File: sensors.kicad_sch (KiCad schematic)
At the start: 43 parts, among them IC1 SHT40-CD1B-R3, IC2 SGP40-D-R4, IC3 SGP40-D-R4, IC4 SGP40-D-R4, IC6 SGP40-D-R4, U2 TCA9546APWR, U3 BMP581, U4 BMP581, U5 BMP581, U6 BMP581

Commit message: feat: pullup resistors values
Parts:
- added R1: 10k, Resistor_SMD:R_0603_1608Metric, symbol Device:R
- R14, R15, R16, R17, R18, R19, R3, R4: value R -> 2k2
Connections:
- net +3V3: now also R1.1
- net ~{RESET}: now also R1.2
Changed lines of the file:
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@@
 	)
 	(junction
+		(at 328.93 143.51)
+		(diameter 0)
+		(color 0 0 0 0)
+	)
+	(junction
 		(at 193.04 242.57)
 		(diameter 0)
@@
 	(polyline
 		(pts
-			(xy 315.722 80.518) (xy 315.722 212.598)
+			(xy 311.912 80.518) (xy 311.912 212.598)
 		)
 		(stroke
@@
 	(polyline
 		(pts
-			(xy 315.722 212.598) (xy 394.462 212.598)
+			(xy 311.912 212.598) (xy 394.462 212.598)
 		)
 		(stroke
@@
 	(wire
 		(pts
+			(xy 328.93 143.51) (xy 337.82 143.51)
+		)
+		(stroke
+			(width 0)
+			(type default)
+		)
+	)
+	(wire
+		(pts
 			(xy 114.3 60.96) (xy 115.57 60.96)
 		)
@@
 	(wire
 		(pts
+			(xy 328.93 134.62) (xy 328.93 143.51)
+		)
+		(stroke
+			(width 0)
+			(type default)
+		)
+	)
+	(wire
+		(pts
 			(xy 193.04 193.04) (xy 193.04 194.31)
 		)
@@
 	(wire
 		(pts
-			(xy 326.39 135.89) (xy 337.82 135.89)
+			(xy 325.12 135.89) (xy 337.82 135.89)
 		)
 		(stroke
@@
 	(wire
 		(pts
+			(xy 328.93 125.73) (xy 328.93 127)
+		)
+		(stroke
+			(width 0)
+			(type default)
+		)
+	)
+	(wire
+		(pts
 			(xy 55.88 116.84) (xy 55.88 125.73)
 		)
@@
 	(wire
 		(pts
-			(xy 328.93 143.51) (xy 337.82 143.51)
+			(xy 325.12 143.51) (xy 328.93 143.51)
 		)
 		(stroke
@@
 	(wire
 		(pts
-			(xy 326.39 138.43) (xy 337.82 138.43)
+			(xy 325.12 138.43) (xy 337.82 138.43)
 		)
 		(stroke
@@
 	(wire
 		(pts
-			(xy 321.31 153.67) (xy 337.82 153.67)
+			(xy 320.04 153.67) (xy 337.82 153.67)
 		)
 		(stroke
@@
 	(polyline
 		(pts
-			(xy 315.722 80.518) (xy 394.462 80.518)
+			(xy 311.912 80.518) (xy 394.462 80.518)
 		)
 		(stroke
@@
 	(wire
 		(pts
-			(xy 321.31 156.21) (xy 337.82 156.21)
+			(xy 320.04 156.21) (xy 337.82 156.21)
 		)
 		(stroke
@@
 	(wire
 		(pts
-			(xy 321.31 151.13) (xy 337.82 151.13)
+			(xy 320.04 151.13) (xy 337.82 151.13)
 		)
 		(stroke
@@
 	(text "I2C SWITCH"
 		(exclude_from_sim no)
-		(at 321.056 79.756 0)
+		(at 317.246 79.756 0)
 		(effects
 			(font
@@
 	)
 	(label "A2"
-		(at 321.31 151.13 0)
+		(at 320.04 151.13 0)
 		(effects
 			(font
@@
 	)
 	(label "A0"
-		(at 321.31 156.21 0)
+		(at 320.04 156.21 0)
 		(effects
 			(font
@@
 	)
 	(label "A1"
-		(at 321.31 153.67 0)
+		(at 320.04 153.67 0)
 		(effects
 			(font
@@
 	(hierarchical_label "SDA"
 		(shape bidirectional)
-		(at 326.39 135.89 180)
+		(at 325.12 135.89 180)
 		(effects
 			(font
@@
 	(hierarchical_label "SCK"
 		(shape input)
-		(at 326.39 138.43 180)
+		(at 325.12 138.43 180)
 		(effects
 			(font
@@
 	(hierarchical_label "~{RESET}"
 		(shape input)
-		(at 328.93 143.51 180)
+		(at 325.12 143.51 180)
 		(effects
 			(font
@@
 			)
 		)
-		(property "Value" "R"
+		(property "Value" "2k2"
 			(at 68.834 177.8 0)
 			(effects
@@
 	)
 	(symbol
+		(lib_id "Device:R")
+		(at 328.93 130.81 0)
+		(unit 1)
+		(exclude_from_sim no)
+		(in_bom yes)
+		(on_board yes)
+		(dnp no)
+		(property "Reference" "R1"
+			(at 330.962 129.54 0)
+			(effects
+				(font
+					(size 1.27 1.27)
+				)
+				(justify left)
+			)
+		)
+		(property "Value" "10k"
+			(at 330.962 131.826 0)
+			(effects
+				(font
+					(size 1.27 1.27)
+				)
+				(justify left)
+			)
+		)
+		(property "Footprint" "Resistor_SMD:R_0603_1608Metric"
+			(at 327.152 130.81 90)
+			(effects
+				(font
+					(size 1.27 1.27)
+				)
+				(hide yes)
+			)
+		)
+		(property "Datasheet" "~"
+			(at 328.93 130.81 0)
+			(effects
+				(font
+					(size 1.27 1.27)
+				)
+				(hide yes)
+			)
+		)
+		(property "Description" "Resistor"
+			(at 328.93 130.81 0)
+			(effects
+				(font
+					(size 1.27 1.27)
+				)
+				(hide yes)
+			)
+		)
+		(pin "2"
+		)
+		(pin "1"
+		)
+		(instances
+			(project "kiba"
+				(path "/830d4d2d-479f-4d6d-bef5-9f1041d3fb90/20f4cbdc-d1db-4d2f-acce-cbdfb89574ee"
+					(reference "R1")
+					(unit 1)
+				)
+			)
+		)
+	)
+	(symbol
 		(lib_id "Device:C")
 		(at 339.09 113.03 0)
@@
 			)
 		)
-		(property "Value" "R"
+		(property "Value" "2k2"
 			(at 81.28 50.7999 0)
 			(effects
@@
 			)
 		)
-		(property "Value" "R"
+		(property "Value" "2k2"
 			(at 68.834 114.3 0)
 			(effects
@@
 			)
 		)
-		(property "Value" "R"
+		(property "Value" "2k2"
 			(at 81.28 238.7599 0)
 			(effects
@@
 	)
 	(symbol
+		(lib_id "power:+3V3")
+		(at 328.93 125.73 0)
+		(unit 1)
+		(exclude_from_sim no)
+		(in_bom yes)
+		(on_board yes)
+		(dnp no)
+		(property "Reference" "#PWR6"
+			(at 328.93 129.54 0)
+			(effects
+				(font
+					(size 1.27 1.27)
+				)
+				(hide yes)
+			)
+		)
+		(property "Value" "+3V3"
+			(at 328.93 121.92 0)
+			(effects
+				(font
+					(size 1.27 1.27)
+				)
+			)
+		)
+		(property "Footprint" ""
+			(at 328.93 125.73 0)
+			(effects
+				(font
+					(size 1.27 1.27)
+				)
+				(hide yes)
+			)
+		)
+		(property "Datasheet" ""
+			(at 328.93 125.73 0)
+			(effects
+				(font
+					(size 1.27 1.27)
+				)
+				(hide yes)
+			)
+		)
+		(property "Description" "Power symbol creates a global label with name \"+3V3\""
+			(at 328.93 125.73 0)
+			(effects
+				(font
+					(size 1.27 1.27)
+				)
+				(hide yes)
+			)
+		)
+		(pin "1"
+		)
+		(instances
+			(project "kiba"
+				(path "/830d4d2d-479f-4d6d-bef5-9f1041d3fb90/20f4cbdc-d1db-4d2f-acce-cbdfb89574ee"
+					(reference "#PWR6")
+					(unit 1)
+				)
+			)
+		)
+	)
+	(symbol
 		(lib_id "Device:R")
 		(at 171.45 102.87 0)
@@
 			)
 		)
-		(property "Value" "R"
+		(property "Value" "2k2"
 			(at 81.28 177.7999 0)
 			(effects
@@
 			)
 		)
-		(property "Value" "R"
+		(property "Value" "2k2"
 			(at 68.834 238.76 0)
 			(effects
@@
 			)
 		)
-		(property "Value" "R"
+		(property "Value" "2k2"
 			(at 68.834 50.8 0)
 			(effects
@@
 			)
 		)
-		(property "Value" "R"
+		(property "Value" "2k2"
 			(at 81.28 114.2999 0)
 			(effects

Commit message: Added JLCPCB part numbers and generated BOM
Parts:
- IC1: LCSC (none) -> C7461852
- IC2, IC3, IC4, IC6: LCSC (none) -> C2874215
- U2: LCSC (none) -> C201653
- U3, U4, U5, U6: LCSC (none) -> C5362283
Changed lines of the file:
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@@
 			)
 		)
+		(property "LCSC" "C2874215"
+			(at 193.04 63.5 0)
+			(effects
+				(font
+					(size 1.27 1.27)
+				)
+				(hide yes)
+			)
+		)
 		(pin "1"
 		)
@@
 			)
 		)
+		(property "LCSC" "C5362283"
+			(at 114.3 240.0614 0)
+			(effects
+				(font
+					(size 1.27 1.27)
+				)
+				(hide yes)
+			)
+		)
 		(pin "10"
 		)
@@
 			)
 		)
+		(property "LCSC" "C5362283"
+			(at 114.3 179.1014 0)
+			(effects
+				(font
+					(size 1.27 1.27)
+				)
+				(hide yes)
+			)
+		)
 		(pin "10"
 		)
@@
 			)
 		)
+		(property "LCSC" "C201653"
+			(at 354.33 118.11 0)
+			(effects
+				(font
+					(size 1.27 1.27)
+				)
+				(hide yes)
+			)
+		)
 		(pin "3"
 		)
@@
 			)
 		)
+		(property "LCSC" "C7461852"
+			(at 275.59 138.43 0)
+			(effects
+				(font
+					(size 1.27 1.27)
+				)
+				(hide yes)
+			)
+		)
 		(pin "1"
 		)
@@
 			)
 		)
+		(property "LCSC" "C2874215"
+			(at 193.04 215.9 0)
+			(effects
+				(font
+					(size 1.27 1.27)
+				)
+				(hide yes)
+			)
+		)
 		(pin "1"
 		)
@@
 			)
 		)
+		(property "LCSC" "C5362283"
+			(at 114.3 115.6014 0)
+			(effects
+				(font
+					(size 1.27 1.27)
+				)
+				(hide yes)
+			)
+		)
 		(pin "10"
 		)
@@
 			)
 		)
+		(property "LCSC" "C2874215"
+			(at 193.04 107.95 0)
+			(effects
+				(font
+					(size 1.27 1.27)
+				)
+				(hide yes)
+			)
+		)
 		(pin "1"
 		)
@@
 			)
 		)
+		(property "LCSC" "C5362283"
+			(at 114.3 52.1014 0)
+			(effects
+				(font
+					(size 1.27 1.27)
+				)
+				(hide yes)
+			)
+		)
 		(pin "10"
 		)
@@
 				(hide yes)
 			)
+		)
+		(property "LCSC" "C2874215"
+			(at 193.04 166.37 0)
+			(effects
+				(font
+					(size 1.27 1.27)
+				)
+				(hide yes)
+			)

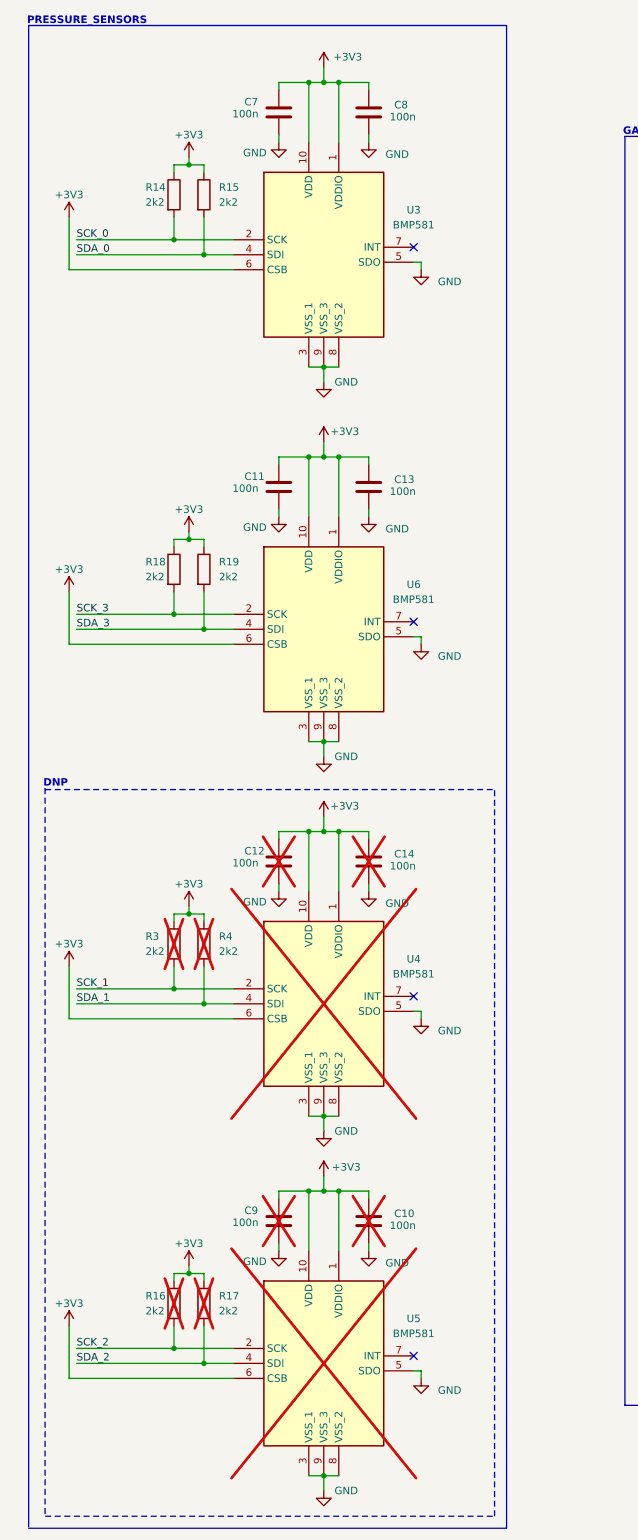
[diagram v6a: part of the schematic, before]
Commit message: fix: cps135b as new barometer
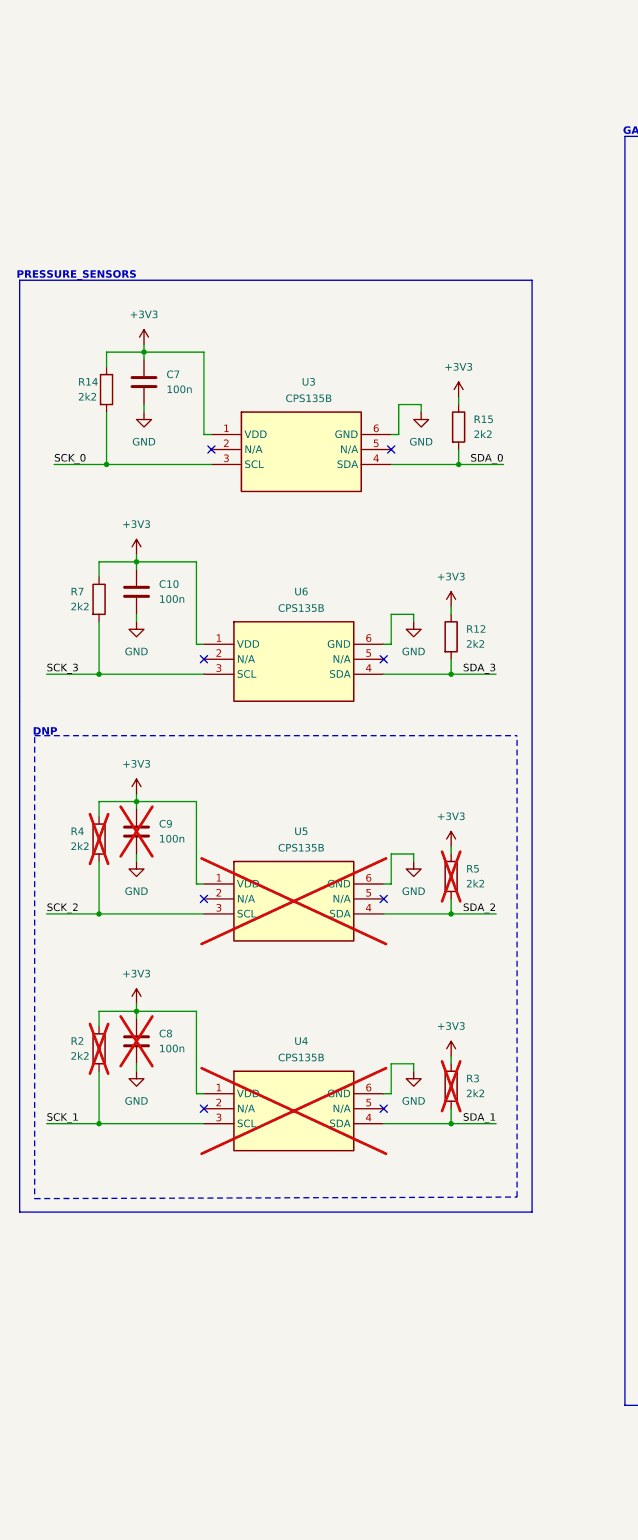
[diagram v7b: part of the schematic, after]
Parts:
- removed C11, C12, C13, C14: 100n, Capacitor_SMD:C_0603_1608Metric, symbol Device:C
- removed R16, R17, R18, R19: 2k2, Resistor_SMD:R_0603_1608Metric, symbol Device:R
- added R12, R2, R5, R7: 2k2, Resistor_SMD:R_0603_1608Metric, symbol Device:R
- C10: now fitted; now in the parts list
- C8: now not fitted; now left out of the parts list
- U3, U4, U5, U6: value BMP581 -> CPS135B; footprint Local:BMP581 -> smd6:smd6-4.5mm
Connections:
- net +3V3: now also R12.1, R2.1, R5.1, R7.1; no longer U3.10 (VDD), U3.6 (CSB), U4.10 (VDD), U4.6 (CSB), U5.10 (VDD), U5.6 (CSB), U6.10 (VDD), U6.6 (CSB)
- net GND: now also U3.6 (GND), U4.6 (GND), U5.6 (GND), U6.6 (GND); no longer U3.3 (VSS_1), U3.5 (SDO), U3.8 (VSS_2), U3.9 (VSS_3), U4.3 (VSS_1), U4.5 (SDO), U4.8 (VSS_2), U4.9 (VSS_3), U5.3 (VSS_1), U5.5 (SDO), U5.8 (VSS_2), U5.9 (VSS_3), U6.3 (VSS_1), U6.5 (SDO), U6.8 (VSS_2), U6.9 (VSS_3)
- net SCK_0: now also U3.3 (SCL); no longer U3.2 (SCK)
- net SCK_1: now also U4.3 (SCL), R2.2; no longer R3.2, U4.2 (SCK)
- net SCK_2: now also R4.2, U5.3 (SCL); no longer U5.2 (SCK)
- net SCK_3: now also U6.3 (SCL), R7.2; no longer U6.2 (SCK)
- net SDA_1: now also R3.2; no longer R4.2
- net SDA_2: now also R5.2
- net SDA_3: now also R12.2
- no-connect marks 4 -> 8
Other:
- moved on the sheet: R14, R15

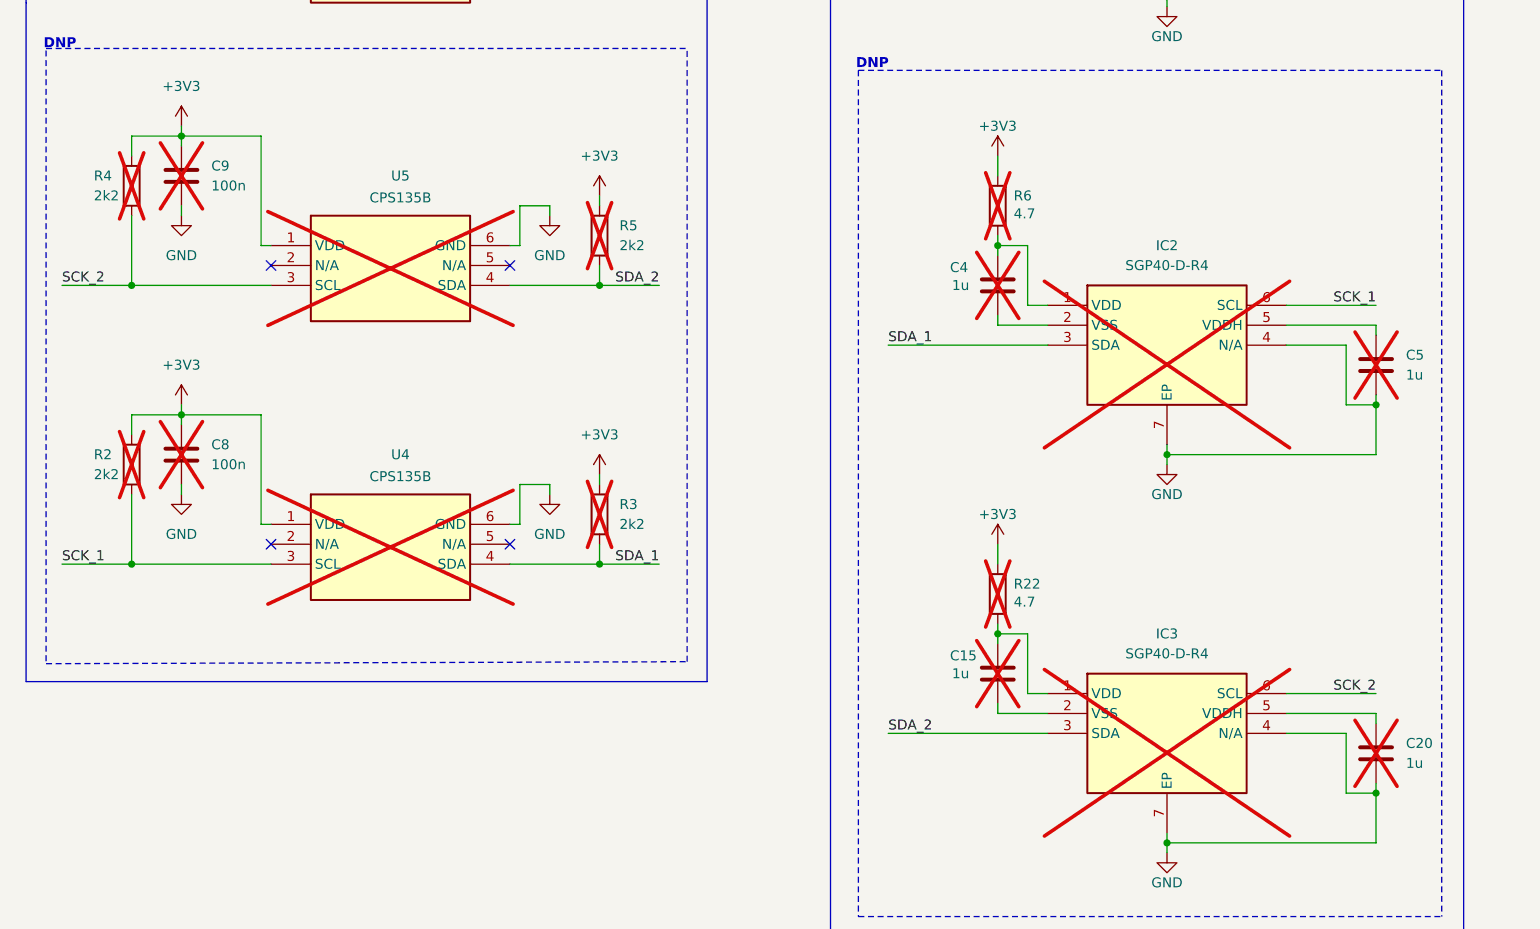
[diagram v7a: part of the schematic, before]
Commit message: production files for jlcpcb, added passives for DNP sensors
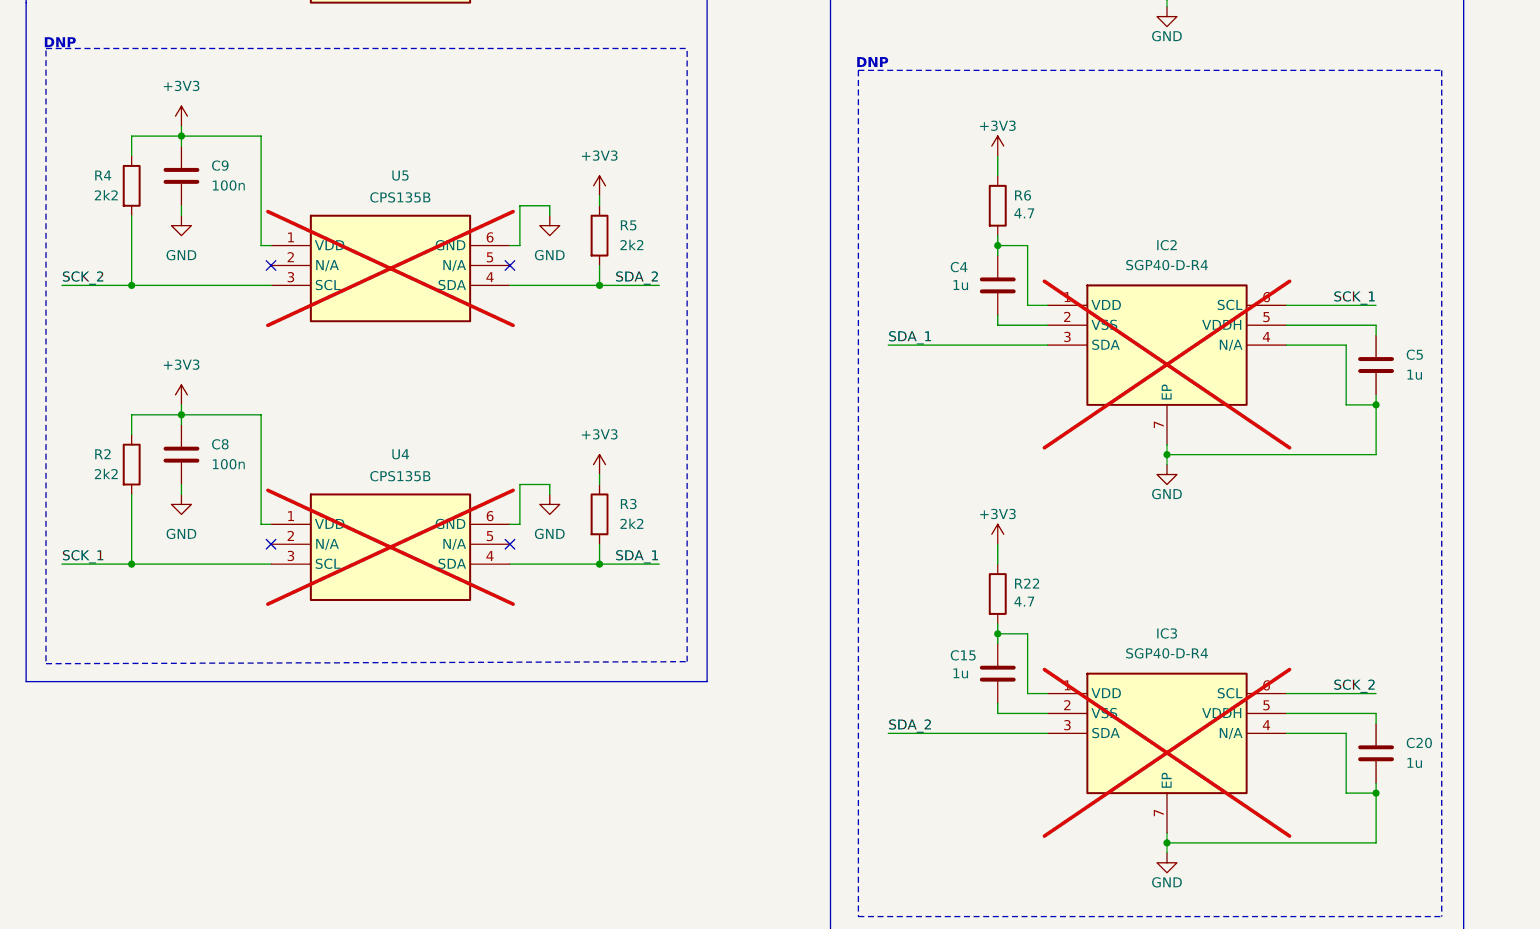
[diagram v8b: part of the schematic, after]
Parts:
- C15, C20, C4, C5, C8, C9, R2, R22, R3, R4, R5, R6: now fitted; now in the parts list
- U3, U4, U5, U6: LCSC C5362283 -> C491452; Manufacturer_Name BOSCH -> (none); Manufacturer_Part_Number BMP581 -> (none); Mouser Part Number 262-BMP581 -> (none); Mouser Price/Stock https://www.mouser.co.uk/ProductDetail/Bosch-Sensortec/BMP5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 -> (none)
